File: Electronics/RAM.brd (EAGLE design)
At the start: 50 x 50 mm, 16 parts, among them IC1 74LS32D, Q1 MMBTA42

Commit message: Fix up caps on ram/mcu board
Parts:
- added C5: (no value), rcl:C0805
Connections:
- net GND: now also C5.2
- net VCC: now also C5.1
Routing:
- net VCC: track 116.9 -> 118.5 mm, vias 4 -> 5
- added copper zone on layer 1, net VCC
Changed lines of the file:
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@@
 <text x="5.715" y="12.7" size="1.016" layer="1" rot="R90">Ben V. Brown</text>
 <text x="1.905" y="12.065" size="1.016" layer="1" rot="R90">RalimTek.com</text>
+<wire x1="49.8475" y1="49.8475" x2="49.8475" y2="0.3175" width="0.254" layer="22"/>
+<wire x1="49.8475" y1="0.3175" x2="0.3175" y2="0.3175" width="0.254" layer="22"/>
+<wire x1="0.3175" y1="0.3175" x2="0.3175" y2="49.8475" width="0.254" layer="22"/>
+<wire x1="0.3175" y1="49.8475" x2="49.8475" y2="49.8475" width="0.254" layer="22"/>
 </plain>
 <attributes>
@@
 <element name="JP5" library="SparkFun" package="1X02" value="hlt" x="1.641971875" y="41.274996875" smashed="yes" rot="R90"/>
 <element name="JP6" library="SparkFun" package="1X02" value="bus" x="48.337034375" y="41.1979625" smashed="yes" rot="R90"/>
+<element name="C5" library="rcl" package="C0805" value="" x="22.225" y="27.94" smashed="yes" rot="MR0">
+<attribute name="VALUE" x="23.495" y="25.4" size="1.27" layer="28" rot="MR0"/>
+</element>
 </elements>
 <signals>
@@
 <wire x1="29.5275" y1="4.7625" x2="29.845" y2="5.08" width="0.3048" layer="16"/>
 <wire x1="29.845" y1="5.08" x2="29.845" y2="7.305" width="0.3048" layer="16"/>
+<polygon width="0.3048" layer="1">
+<vertex x="1.27" y="6.985"/>
+<vertex x="5.08" y="3.175"/>
+<vertex x="5.08" y="1.905"/>
+<vertex x="5.715" y="1.27"/>
+<vertex x="45.085" y="1.27"/>
+<vertex x="45.72" y="1.905"/>
+<vertex x="45.72" y="3.175"/>
+<vertex x="48.895" y="6.35"/>
+<vertex x="48.895" y="43.815"/>
+<vertex x="45.72" y="46.99"/>
+<vertex x="45.72" y="48.26"/>
+<vertex x="45.085" y="48.895"/>
+<vertex x="5.715" y="48.895"/>
+<vertex x="5.08" y="48.26"/>
+<vertex x="5.08" y="46.99"/>
+<vertex x="1.27" y="43.18"/>
+</polygon>
+<contactref element="C5" pad="1"/>
+<wire x1="23.175" y1="27.94" x2="24.13" y2="27.94" width="0.254" layer="16"/>
+<via x="24.13" y="27.94" extent="1-16" drill="0.6" shape="octagon"/>
+<wire x1="24.13" y1="27.94" x2="24.765" y2="27.94" width="0.254" layer="1"/>
 </signal>
 <signal name="GND">
@@
 <wire x1="47.3075" y1="12.065" x2="46.99" y2="12.065" width="0.3048" layer="16"/>
 <contactref element="JP2" pad="9"/>
+<contactref element="C5" pad="2"/>
 </signal>
 <signal name="WE">

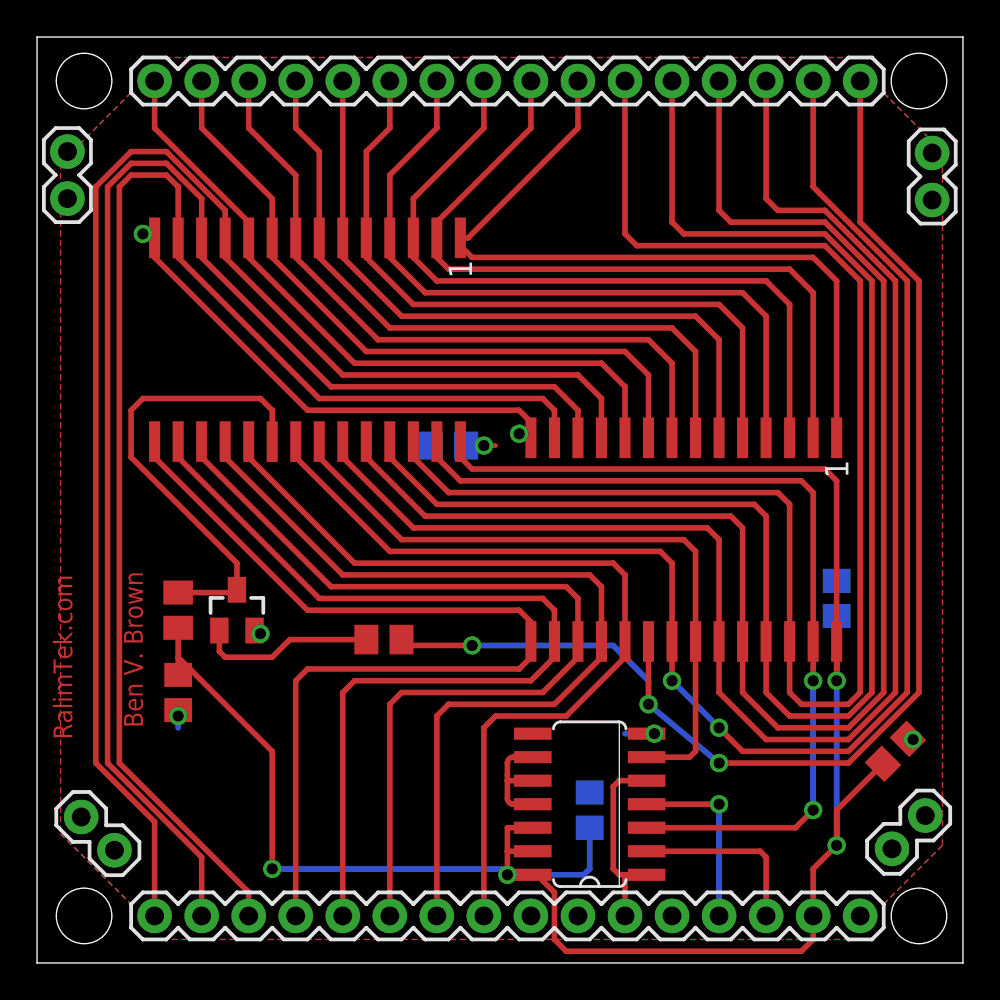
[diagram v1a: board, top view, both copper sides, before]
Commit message: Route DIO Breakout + update Text
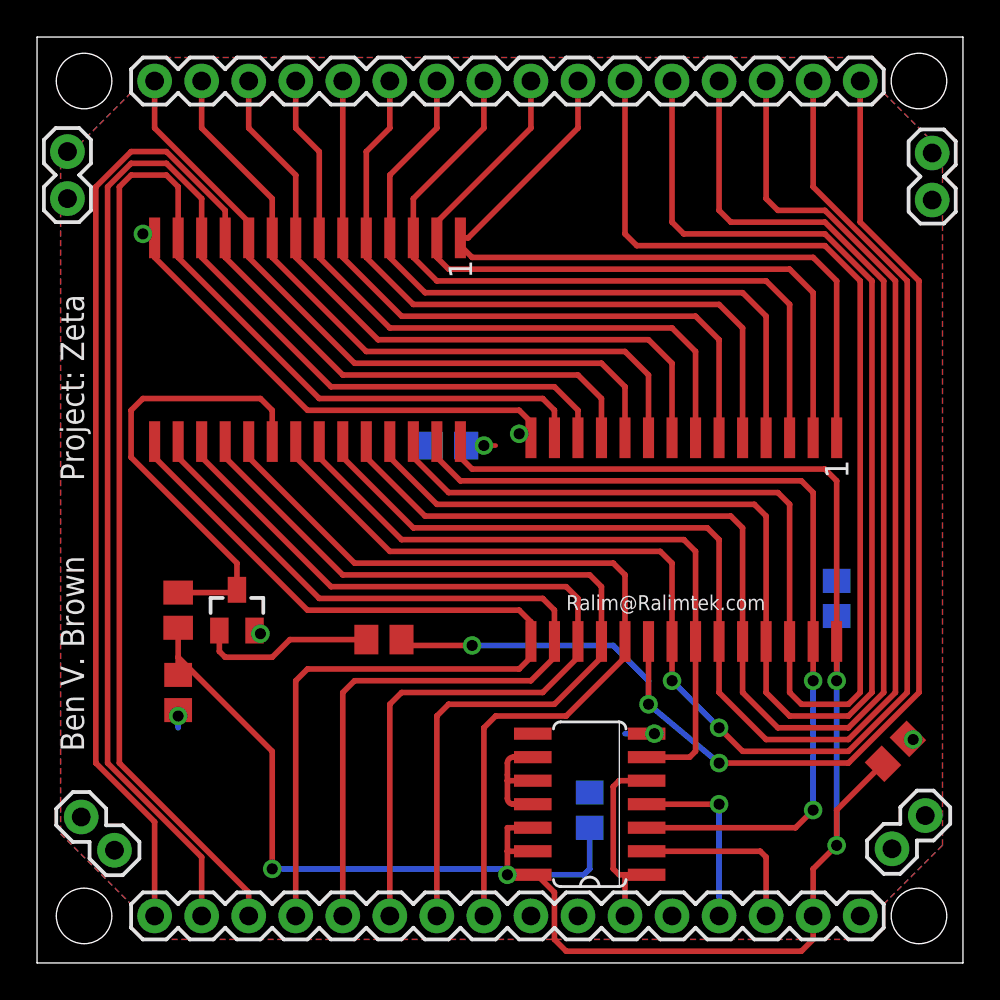
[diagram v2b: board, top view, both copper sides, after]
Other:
- board text added: "Project: Zeta"
- board text added: "Ralim@Ralimtek.com"
- board text removed: "RalimTek.com"
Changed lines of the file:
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@@
 <hole x="47.625" y="2.54" drill="3"/>
 <hole x="2.54" y="2.54" drill="3"/>
-<text x="5.715" y="12.7" size="1.016" layer="1" rot="R90">Ben V. Brown</text>
-<text x="1.905" y="12.065" size="1.016" layer="1" rot="R90">RalimTek.com</text>
 <wire x1="49.8475" y1="49.8475" x2="49.8475" y2="0.3175" width="0.254" layer="22"/>
 <wire x1="49.8475" y1="0.3175" x2="0.3175" y2="0.3175" width="0.254" layer="22"/>
 <wire x1="0.3175" y1="0.3175" x2="0.3175" y2="49.8475" width="0.254" layer="22"/>
 <wire x1="0.3175" y1="49.8475" x2="49.8475" y2="49.8475" width="0.254" layer="22"/>
+<text x="2.54" y="26.035" size="1.27" layer="21" font="vector" rot="R90">Project: Zeta</text>
+<text x="2.54" y="11.43" size="1.27" layer="21" font="vector" rot="R90">Ben V. Brown</text>
+<text x="28.575" y="19.05" size="0.8128" layer="21" font="vector">Ralim@Ralimtek.com</text>
 </plain>
 <attributes>

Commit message: Gerbers!
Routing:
- net GND: track 32.7 -> 30.6 mm
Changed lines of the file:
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@@
 <setting verticaltext="up"/>
 </settings>
-<grid distance="25" unitdist="mil" unit="mil" style="lines" multiple="1" display="no" altdistance="12.5" altunitdist="mil" altunit="mil"/>
+<grid distance="25" unitdist="mil" unit="mm" style="lines" multiple="1" display="no" altdistance="12.5" altunitdist="mil" altunit="mil"/>
 <layers>
 <layer number="1" name="Top" color="4" fill="1" visible="yes" active="yes"/>
@@
 <text x="2.54" y="11.43" size="1.27" layer="21" font="vector" rot="R90">Ben V. Brown</text>
 <text x="28.575" y="19.05" size="0.8128" layer="21" font="vector">Ralim@Ralimtek.com</text>
+<text x="8.255" y="33.655" size="0.8128" layer="21" font="vector">Ralim@Ralimtek.com</text>
 </plain>
 <attributes>
@@
 </class>
 </classes>
-<designrules name="default">
-<description language="de">&lt;b&gt;EAGLE Design Rules&lt;/b&gt;
-&lt;p&gt;
-Die Standard-Design-Rules sind so gewählt, dass sie für
-die meisten Anwendungen passen. Sollte ihre Platine
-besondere Anforderungen haben, treffen Sie die erforderlichen
-Einstellungen hier und speichern die Design Rules unter
-einem neuen Namen ab.</description>
-<description language="en">&lt;b&gt;EAGLE Design Rules&lt;/b&gt;
-&lt;p&gt;
-The default Design Rules have been set to cover
-a wide range of applications. Your particular design
-may have different requirements, so please make the
-necessary adjustments and save your customized
-design rules under a new name.</description>
+<designrules name="dirt_cheap_dirty_boards.v1">
+<description language="en">&lt;b&gt;Dirty Cheap Dirty Board Design Rules&lt;/b&gt;
+&lt;br&gt;
+&lt;br&gt;Min width/Spacing: 5/5mil
+&lt;br&gt;Min diameter of finished hole 12mil</description>
 <param name="layerSetup" value="(1*16)"/>
-<param name="mtCopper" value="0.035mm 0.035mm 0.035mm 0.035mm 0.035mm 0.035mm 0.035mm 0.035mm 0.035mm 0.035mm 0.035mm 0.035mm 0.035mm 0.035mm 0.035mm 0.035mm"/>
-<param name="mtIsolate" value="1.5mm 0.15mm 0.2mm 0.15mm 0.2mm 0.15mm 0.2mm 0.15mm 0.2mm 0.15mm 0.2mm 0.15mm 0.2mm 0.15mm 0.2mm"/>
-<param name="mdWireWire" value="8mil"/>
-<param name="mdWirePad" value="8mil"/>
-<param name="mdWireVia" value="8mil"/>
-<param name="mdPadPad" value="8mil"/>
-<param name="mdPadVia" value="8mil"/>
-<param name="mdViaVia" value="8mil"/>
-<param name="mdSmdPad" value="8mil"/>
-<param name="mdSmdVia" value="8mil"/>
-<param name="mdSmdSmd" value="8mil"/>
+<param name="mtCopper" value="0.035mm 0.0175mm 0.035mm 0.035mm 0.035mm 0.035mm 0.035mm 0.035mm 0.035mm 0.035mm 0.035mm 0.035mm 0.035mm 0.035mm 0.0175mm 0.035mm"/>
+<param name="mtIsolate" value="1.5mm 1.1mm 0.2mm 0.15mm 0.2mm 0.15mm 0.2mm 0.15mm 0.2mm 0.15mm 0.2mm 0.15mm 0.2mm 0.15mm 0.2mm"/>
+<param name="mdWireWire" value="5mil"/>
+<param name="mdWirePad" value="5mil"/>
+<param name="mdWireVia" value="5mil"/>
+<param name="mdPadPad" value="5mil"/>
+<param name="mdPadVia" value="5mil"/>
+<param name="mdViaVia" value="5mil"/>
+<param name="mdSmdPad" value="0mil"/>
+<param name="mdSmdVia" value="0mil"/>
+<param name="mdSmdSmd" value="0mil"/>
 <param name="mdViaViaSameLayer" value="8mil"/>
 <param name="mnLayersViaInSmd" value="2"/>
-<param name="mdCopperDimension" value="40mil"/>
-<param name="mdDrill" value="8mil"/>
+<param name="mdCopperDimension" value="10mil"/>
+<param name="mdDrill" value="10mil"/>
 <param name="mdSmdStop" value="0mil"/>
-<param name="msWidth" value="10mil"/>
-<param name="msDrill" value="24mil"/>
-<param name="msMicroVia" value="9.99mm"/>
+<param name="msWidth" value="5mil"/>
+<param name="msDrill" value="12mil"/>
+<param name="msMicroVia" value="12mil"/>
 <param name="msBlindViaRatio" value="0.5"/>
 <param name="rvPadTop" value="0.25"/>
@@
 <param name="rlMinPadBottom" value="10mil"/>
 <param name="rlMaxPadBottom" value="20mil"/>
-<param name="rlMinViaOuter" value="8mil"/>
+<param name="rlMinViaOuter" value="6mil"/>
 <param name="rlMaxViaOuter" value="20mil"/>
-<param name="rlMinViaInner" value="8mil"/>
+<param name="rlMinViaInner" value="6mil"/>
 <param name="rlMaxViaInner" value="20mil"/>
 <param name="rlMinMicroViaOuter" value="4mil"/>
@@
 <param name="psTop" value="-1"/>
 <param name="psBottom" value="-1"/>
-<param name="psFirst" value="-1"/>
+<param name="psFirst" value="0"/>
 <param name="psElongationLong" value="100"/>
 <param name="psElongationOffset" value="100"/>
 <param name="mvStopFrame" value="1"/>
 <param name="mvCreamFrame" value="0"/>
-<param name="mlMinStopFrame" value="4mil"/>
-<param name="mlMaxStopFrame" value="4mil"/>
+<param name="mlMinStopFrame" value="2mil"/>
+<param name="mlMaxStopFrame" value="2mil"/>
 <param name="mlMinCreamFrame" value="0mil"/>
 <param name="mlMaxCreamFrame" value="0mil"/>
-<param name="mlViaStopLimit" value="0mil"/>
+<param name="mlViaStopLimit" value="25mil"/>
 <param name="srRoundness" value="0"/>
 <param name="srMinRoundness" value="0mil"/>
@@
 <param name="checkAngle" value="0"/>
 <param name="checkFont" value="1"/>
-<param name="checkRestrict" value="1"/>
+<param name="checkRestrict" value="0"/>
 <param name="useDiameter" value="13"/>
 <param name="maxErrors" value="50"/>
@@
 </polygon>
 <wire x1="26.67" y1="28.36" x2="26.455" y2="28.575" width="0.3048" layer="1"/>
-<wire x1="26.455" y1="28.575" x2="26.035" y2="28.575" width="0.3048" layer="1"/>
-<via x="26.035" y="28.575" extent="1-16" drill="0.6" shape="octagon"/>
-<wire x1="26.035" y1="28.575" x2="26.67" y2="28.575" width="0.3048" layer="16"/>
+<wire x1="26.455" y1="28.575" x2="26.3525" y2="28.575" width="0.3048" layer="1"/>
+<via x="26.3525" y="28.575" extent="1-16" drill="0.6" shape="octagon"/>
+<wire x1="26.3525" y1="28.575" x2="26.67" y2="28.575" width="0.3048" layer="16"/>
 <wire x1="14.605" y1="29.845" x2="6.35" y2="38.1" width="0.3048" layer="1"/>
 <wire x1="6.35" y1="39.155" x2="6.35" y2="39.37" width="0.3048" layer="1"/>
@@
 <wire x1="5.715" y1="39.37" x2="6.35" y2="39.37" width="0.3048" layer="16"/>
 <wire x1="11.745" y1="17.95" x2="11.915" y2="17.78" width="0.3048" layer="1"/>
-<wire x1="11.915" y1="17.78" x2="12.065" y2="17.78" width="0.3048" layer="1"/>
-<via x="12.065" y="17.78" extent="1-16" drill="0.6" shape="octagon"/>
-<wire x1="7.62" y1="13.655" x2="7.62" y2="13.335" width="0.3048" layer="1"/>
-<via x="7.62" y="13.335" extent="1-16" drill="0.6" shape="octagon"/>
-<wire x1="7.62" y1="13.335" x2="7.62" y2="12.7" width="0.3048" layer="16"/>
+<wire x1="11.915" y1="17.78" x2="11.7475" y2="17.78" width="0.3048" layer="1"/>
+<via x="11.7475" y="17.78" extent="1-16" drill="0.6" shape="octagon"/>
+<wire x1="7.62" y1="13.655" x2="7.62" y2="13.6525" width="0.3048" layer="1"/>
+<via x="7.62" y="13.6525" extent="1-16" drill="0.6" shape="octagon"/>
 <wire x1="32.9184" y1="12.3825" x2="33.3375" y2="12.3825" width="0.3048" layer="1"/>
 <via x="33.3375" y="12.3825" extent="1-16" drill="0.6" shape="octagon"/>
 <wire x1="33.3375" y1="12.3825" x2="31.75" y2="12.3825" width="0.3048" layer="16"/>
-<wire x1="47.02675" y1="12.10175" x2="47.3075" y2="12.065" width="0.3048" layer="1"/>
-<via x="47.3075" y="12.065" extent="1-16" drill="0.6" shape="octagon"/>
-<wire x1="47.3075" y1="12.065" x2="46.99" y2="12.065" width="0.3048" layer="16"/>
+<wire x1="47.02675" y1="12.10175" x2="46.99" y2="12.065" width="0.3048" layer="1"/>
+<via x="46.99" y="12.065" extent="1-16" drill="0.6" shape="octagon"/>
 <contactref element="JP2" pad="9"/>
 <contactref element="C5" pad="2"/>
